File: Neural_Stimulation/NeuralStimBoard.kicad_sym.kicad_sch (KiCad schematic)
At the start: 59 parts, among them U1 CSI040

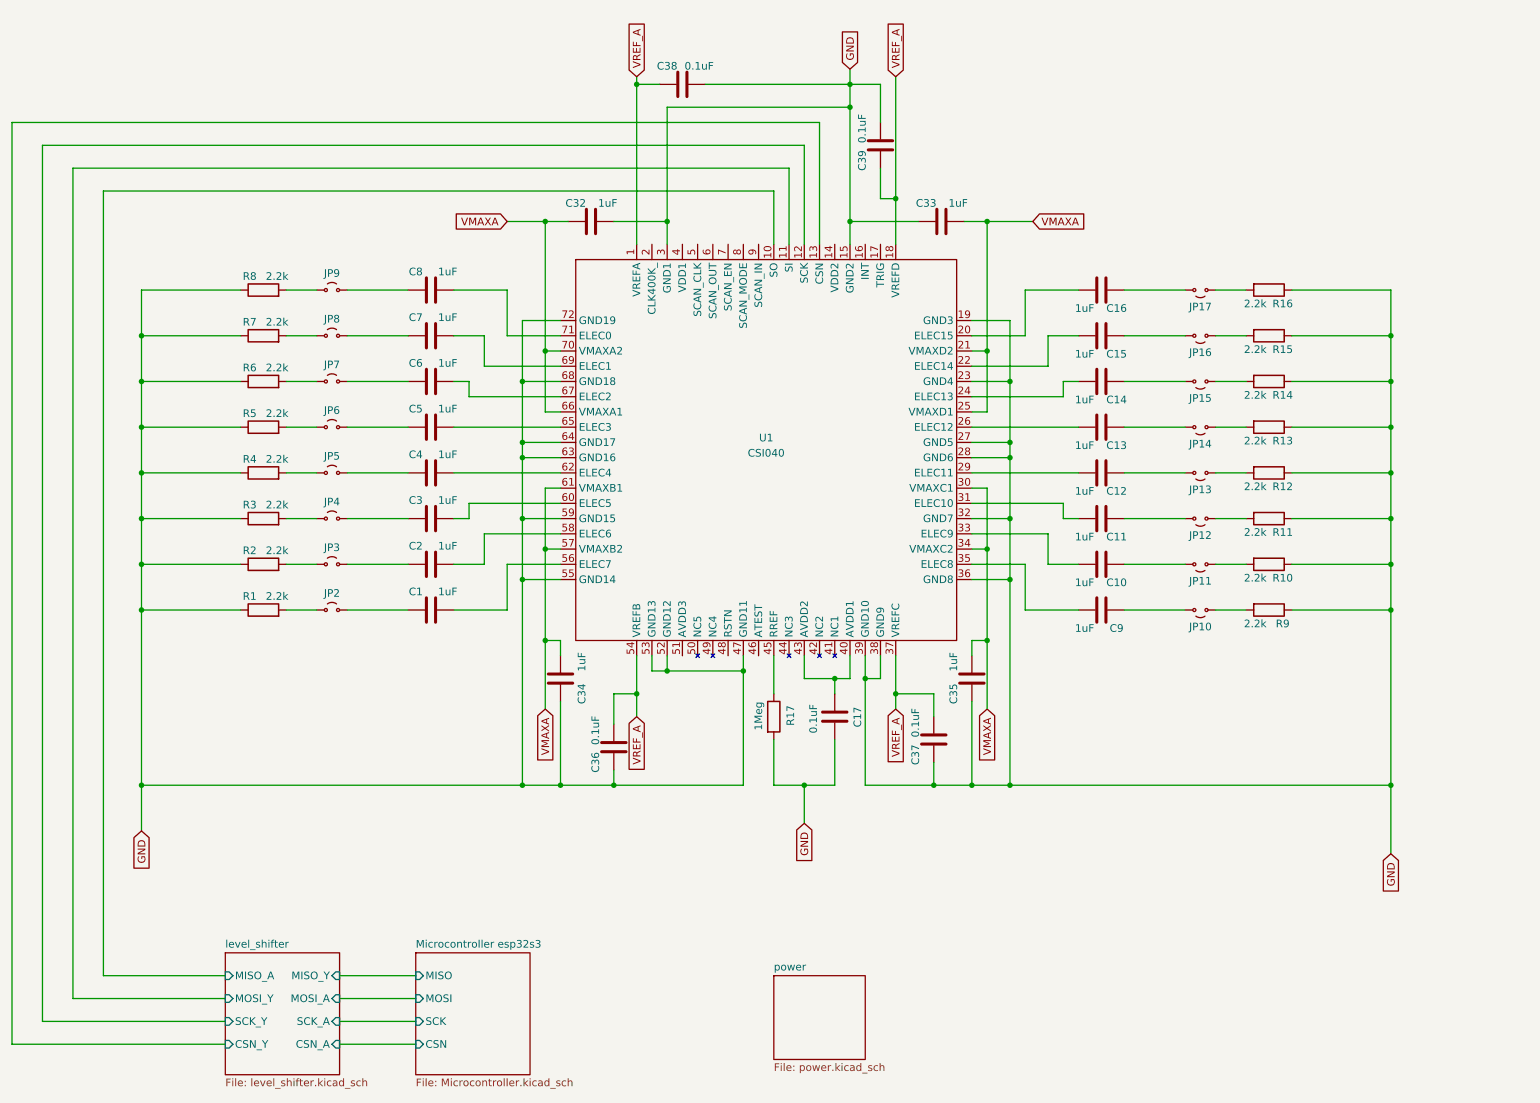
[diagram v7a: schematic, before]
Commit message: Added VDD connections to CSI040
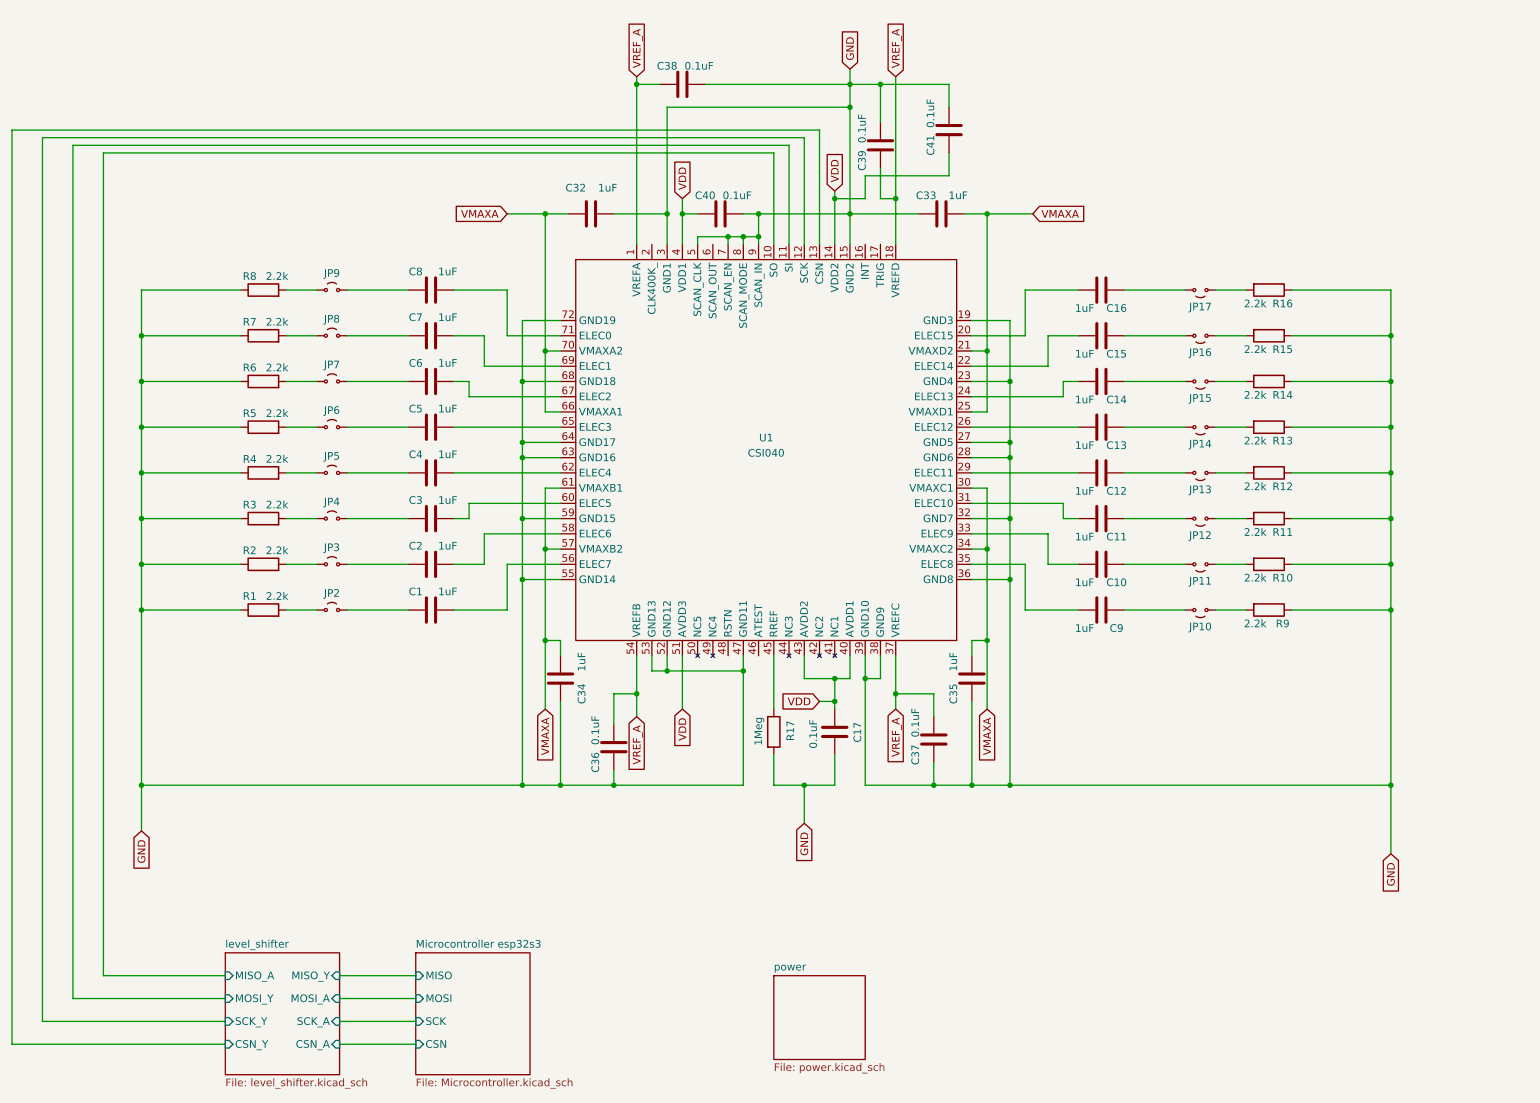
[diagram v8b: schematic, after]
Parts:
- added C40, C41: 0.1uF, symbol Device:C
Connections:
- net GND: now also U1.5 (SCAN_CLK), U1.7 (SCAN_EN), U1.8 (SCAN_MODE), U1.9 (SCAN_IN), C40.2, C41.2
- net VDD: now reaches U1.14 (VDD2)
- net VDD: now also C17.1, U1.4 (VDD1), U1.40 (AVDD1), U1.43 (AVDD2), U1.51 (AVDD3), C40.1, C41.1
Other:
- moved on the sheet: C17, C32, C33, R17
